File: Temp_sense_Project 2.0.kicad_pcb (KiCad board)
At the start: 2 copper layers, 220 x 99 mm, 197 parts, among them J1 348260240, J10 348260240, J11 348260240, J13 348260240, J2 348260240, J3 348260240, J4 348260240, J5 348260240, J6 348260240, J7 Conn_02x08_Odd_Even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

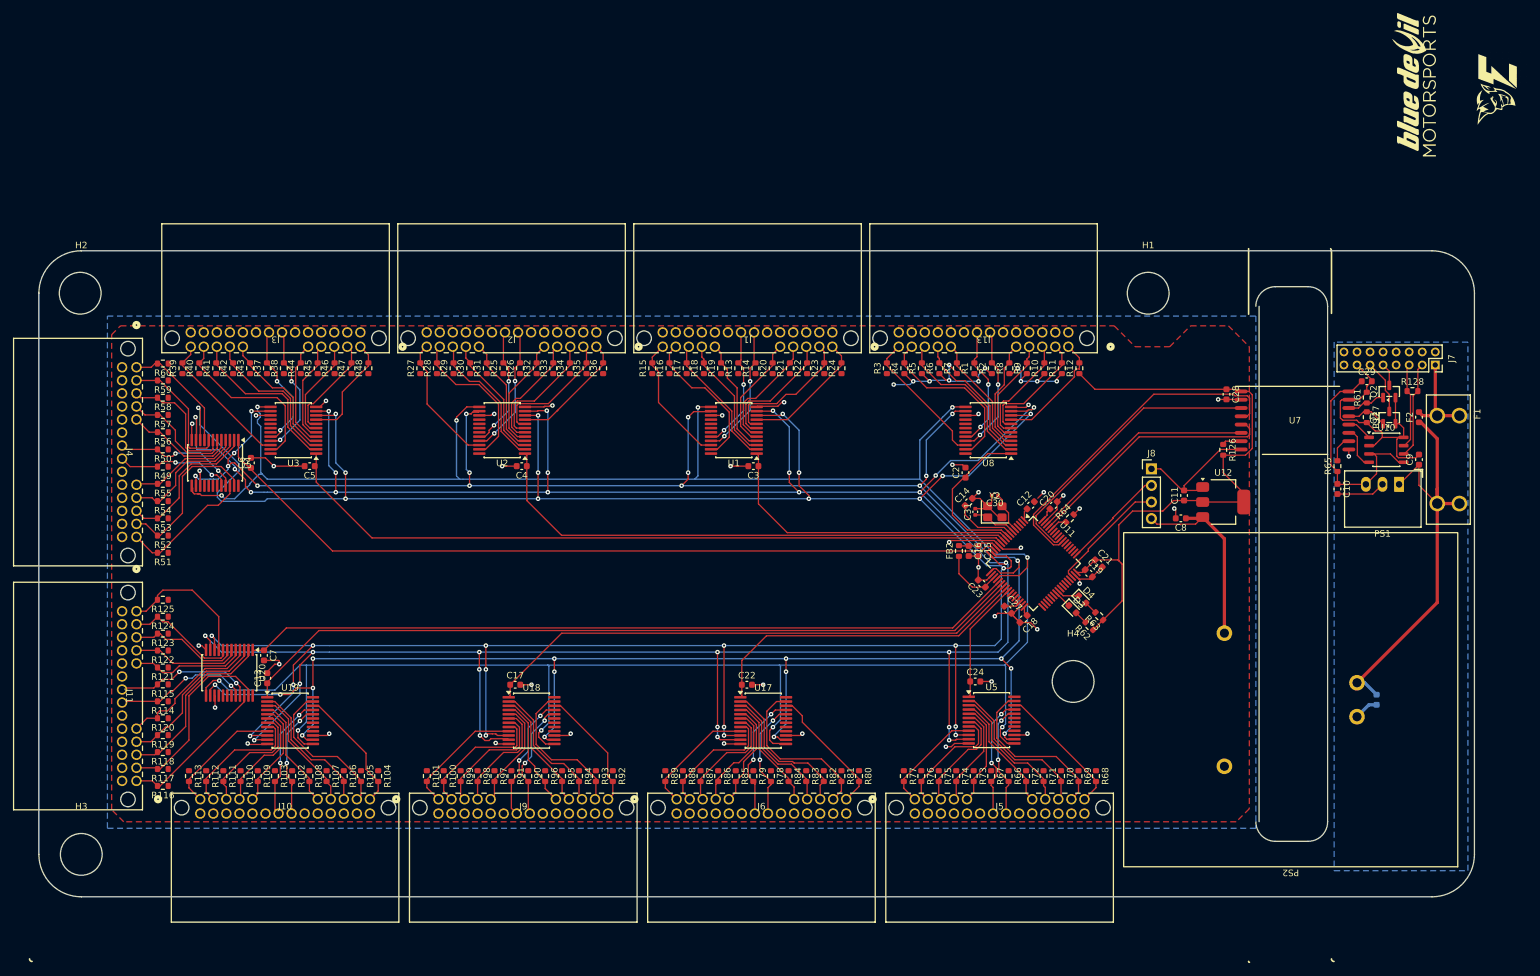
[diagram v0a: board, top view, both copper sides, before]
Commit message: pcb file changed to not error out kicad
also finished a few routes I missed
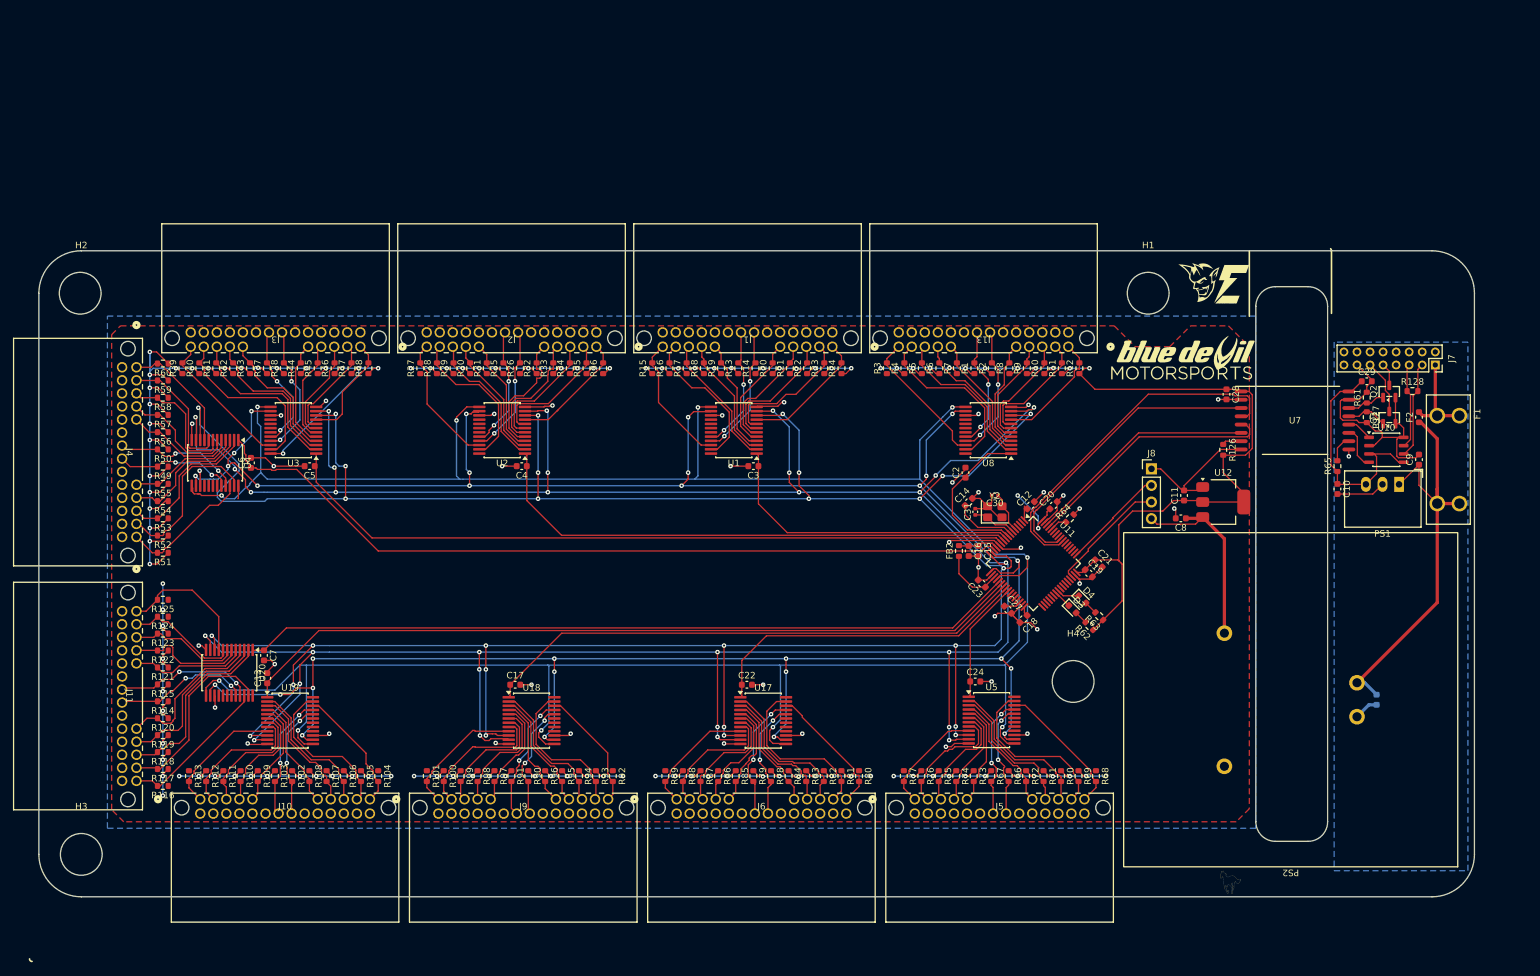
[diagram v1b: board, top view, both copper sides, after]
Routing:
- net +3V3: track 153.8 -> 659.5 mm, vias 11 -> 120
- net Net-(U2-I4): track 17.7 -> 19.7 mm
- net /MCU/Charge Fault: track 52.5 -> 54.2 mm
- net Net-(U20-I3): track 16.7 -> 18.4 mm
- net /MCU/Discharge Fault: track 44.7 -> 46.3 mm
- net Net-(U20-I5): track 22.3 -> 23.9 mm
- net Net-(U20-I6): track 24.5 -> 25.7 mm
- net Net-(U2-I3): track 18.0 -> 19.2 mm
- net Net-(U20-I7): track 27.2 -> 28.1 mm
- net Net-(U3-I6): track 23.3 -> 24.1 mm
- net Net-(U19-I6): track 19.1 -> 19.7 mm
- net Net-(U5-I6): track 21.0 -> 21.6 mm
- net /MCU/S0: track 435.1 -> 435.6 mm
- net /MCU/S3: track 400.6 -> 400.0 mm
- net Net-(U5-I1): track 18.2 -> 18.7 mm
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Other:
- outline, holes or cut-outs redrawn
